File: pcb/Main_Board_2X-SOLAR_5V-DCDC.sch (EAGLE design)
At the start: 69 parts, among them CN5 USBA_FEMALE, IC1 MCP73871, IC2 MCP73871, T2 MMUN2133LT1G, U3 TPS61090RSAR, X1 Solar input, X2 5V output

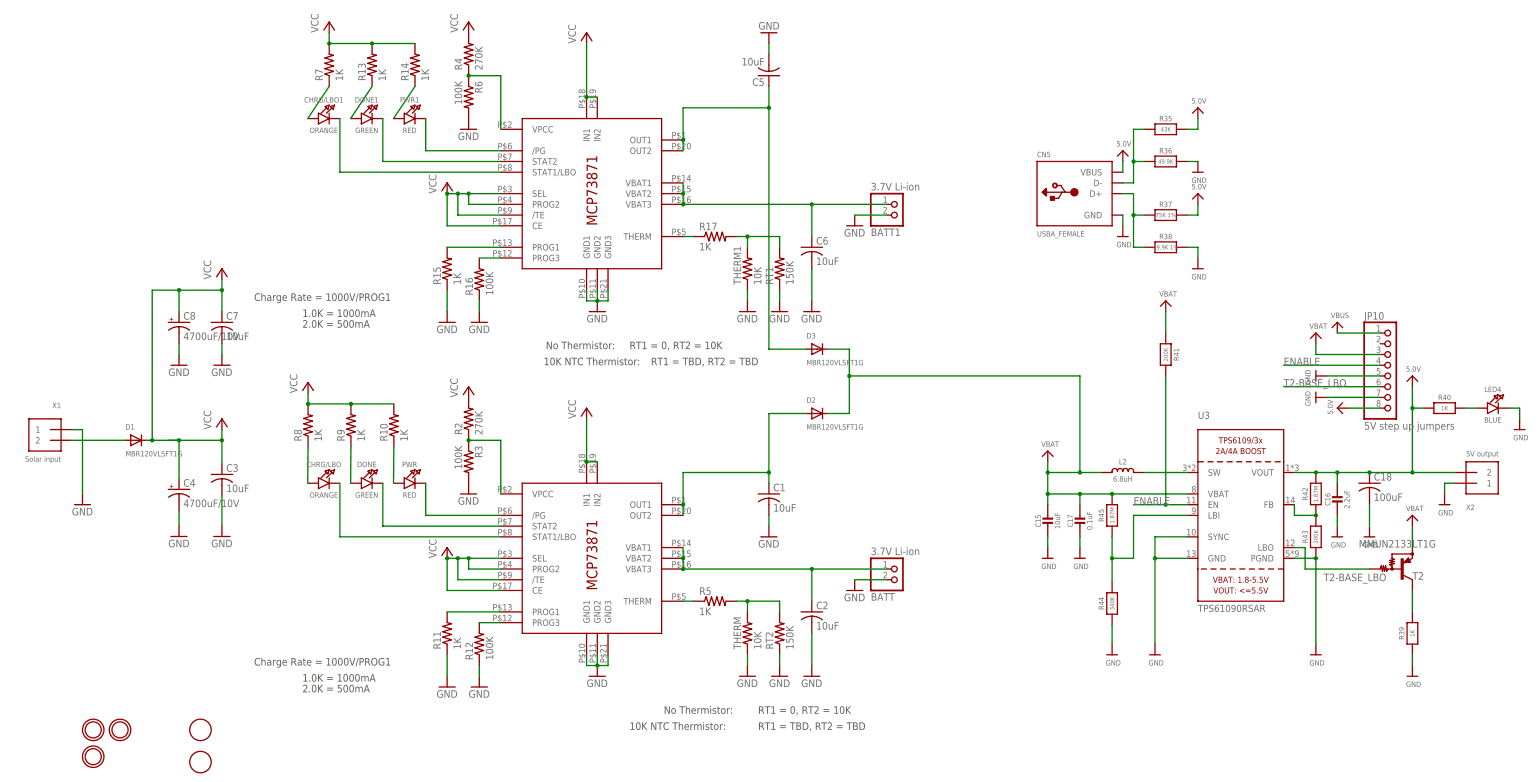
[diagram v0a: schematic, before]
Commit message: Added LT4015 footprints to eagle and began routing
LTC4015 chip footprints and schematic uploaded to eagle library. Routing started for new board. Removed all routings so only airwires exist at this point.
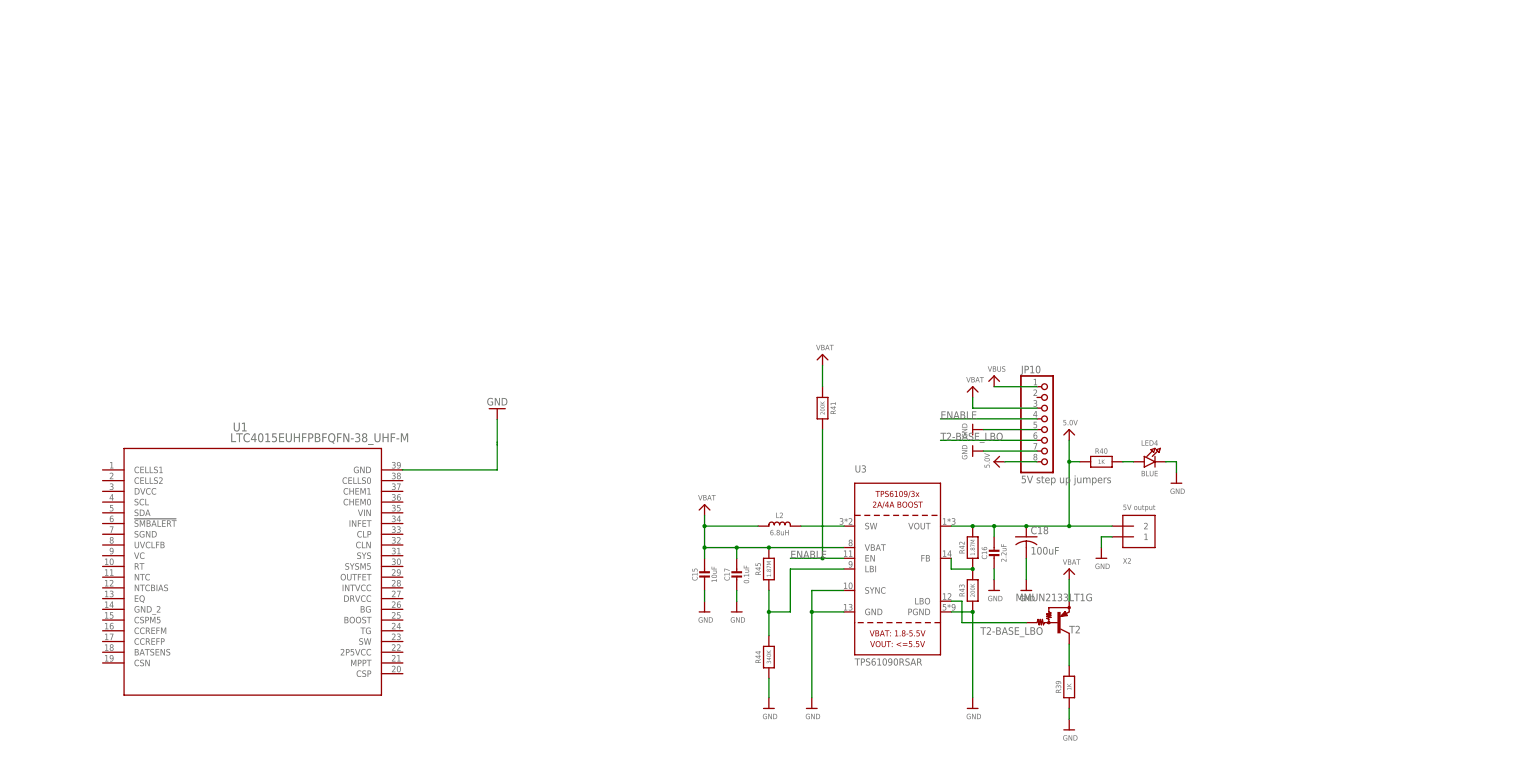
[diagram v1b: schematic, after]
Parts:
- removed BATT, BATT1: 3.7V Li-ion, adafruit:JST_2PIN-SMT-RA
- removed C1, C2, C3, C5, C6, C7: 10uF, adafruit:C-USC0805K
- removed C4, C8: 4700uF/10V, adafruit:CPOL-USE5-13
- removed CHRG/LBO, CHRG/LBO1: ORANGE, microbuilder:LED0805_NOOUTLINE
- removed CN5: USBA_FEMALE, microbuilder:USB_TYPEAPTHFML
- removed D1, D2, D3: MBR120VLSFT1G, microbuilder:DIODESOD-123
- removed DONE, DONE1: GREEN, microbuilder:LED0805_NOOUTLINE
- removed IC1, IC2: MCP73871, adafruit:MCP73871
- removed PWR, PWR1: RED, microbuilder:LED0805_NOOUTLINE
- removed R10, R13, R14, R7, R8, R9: 1K, adafruit:R-US_R0805
- removed R11, R15: 1K, adafruit:R-US_FLIPFLOP
- removed R12, R16, R3, R6: 100K, adafruit:R-US_R0805
- removed R17, R5: 1K, adafruit:R-US_M0805
- removed R2, R4: 270K, adafruit:R-US_R0805
- removed R35: 43K, microbuilder:RESISTOR0805_NOOUTLINE
- removed R36: 49.9K, microbuilder:RESISTOR0805_NOOUTLINE
- removed R37: 75K 1%, microbuilder:RESISTOR0805_NOOUTLINE
- removed R38: 49.9K 1%, microbuilder:RESISTOR0805_NOOUTLINE
- removed RT1, RT2: 150K, adafruit:R-US_M0805
- removed THERM, THERM1: 10K, adafruit:R-US_FLIPFLOP
- removed U$1, U$4, U$6: MOUNTINGHOLE2.5, microbuilder:MOUNTINGHOLE2.5
- removed U$3, U$8: FIDUCIAL, adafruit:FIDUCIAL
- removed X1: Solar input, microbuilder:TERMBLOCK_1X2
- added U1: LTC4015EUHFPBFQFN-38_UHF-M, LTC4015_LTC4015EUHF&hash_PBF:LTC4015EUHFPBFQFN-38_UHF-M
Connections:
- removed net BATT: BATT.2, C2.1, IC1.VBAT1, IC1.VBAT2, IC1.VBAT3
- removed net BATT1: BATT1.2, C6.1, IC2.VBAT1, IC2.VBAT2, IC2.VBAT3
- removed net D+1: CN5.D+, R37.1, R38.1
- removed net D-1: CN5.D-, R35.1, R36.1
- removed net N$12: CHRG/LBO.A, R8.1
- removed net N$13: DONE.A, R9.1
- removed net N$14: PWR.A, R10.1
- removed net N$19: CHRG/LBO1.A, R7.1
- removed net N$20: DONE1.A, R13.1
- removed net N$21: PWR1.A, R14.1
- removed net N$24: IC2.THERM, R17.1
- removed net N$25: R17.2, RT1.2, THERM1.2
- removed net N$5: IC1.THERM, R5.1
- removed net N$8: R5.2, RT2.2, THERM.2
- removed net PG: IC1./PG, PWR.C
- removed net PG_1: IC2./PG, PWR1.C
- removed net PROG1: IC1.PROG1, R11.2
- removed net PROG1_1: IC2.PROG1, R15.2
- removed net PROG3: IC1.PROG3, R12.2
- removed net PROG3_1: IC2.PROG3, R16.2
- removed net PV_IN: D1.A, X1.2
- removed net STAT1: CHRG/LBO.C, IC1.STAT1/LBO
- removed net STAT1_1: CHRG/LBO1.C, IC2.STAT1/LBO
- removed net STAT2: DONE.C, IC1.STAT2
- removed net STAT2_1: DONE1.C, IC2.STAT2
- removed net VCC: C3.1, C4.+, C7.1, C8.+, D1.C, IC1./TE, IC1.CE, IC1.IN1, IC1.IN2, IC1.PROG2, IC1.SEL, IC2./TE, IC2.CE, IC2.IN1, IC2.IN2, IC2.PROG2, IC2.SEL, R10.2, R13.2, R14.2, R2.2, R4.2, R7.2, R8.2, R9.2
- removed net VOUT: C1.1, D2.A, IC1.OUT1, IC1.OUT2
- removed net VOUT1: C5.1, D3.A, IC2.OUT1, IC2.OUT2
- removed net VPCC: IC1.VPCC, R2.1, R3.1
- removed net VPCC1: IC2.VPCC, R4.1, R6.1
- net 5.0V: no longer CN5.VBUS, R35.2, R37.2
- net GND: no longer BATT.1, BATT1.1, C1.2, C2.2, C3.2, C4.-, C5.2, C6.2, C7.2, C8.-, CN5.GND, IC1.GND1, IC1.GND2, IC1.GND3, IC2.GND1, IC2.GND2, IC2.GND3, R11.1, R12.1, R15.1, R16.1, R3.2, R36.2, R38.2, R6.2, RT1.1, RT2.1, THERM.1, THERM1.1, X1.1
- net VBAT: no longer D2.C, D3.C
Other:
- note removed: "1.0K = 1000mA"
- note removed: "10K NTC Thermistor:"
- note removed: "2.0K = 500mA"
- note removed: "Charge Rate = 1000V/PROG1"
- note removed: "No Thermistor:"
- note removed: "RT1 = 0, RT2 = 10K"
- note removed: "RT1 = TBD, RT2 = TBD"
- moved on the sheet: C15, C16, C17, C18, JP10, L2, LED4, R39, R40, R41, R42, R43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

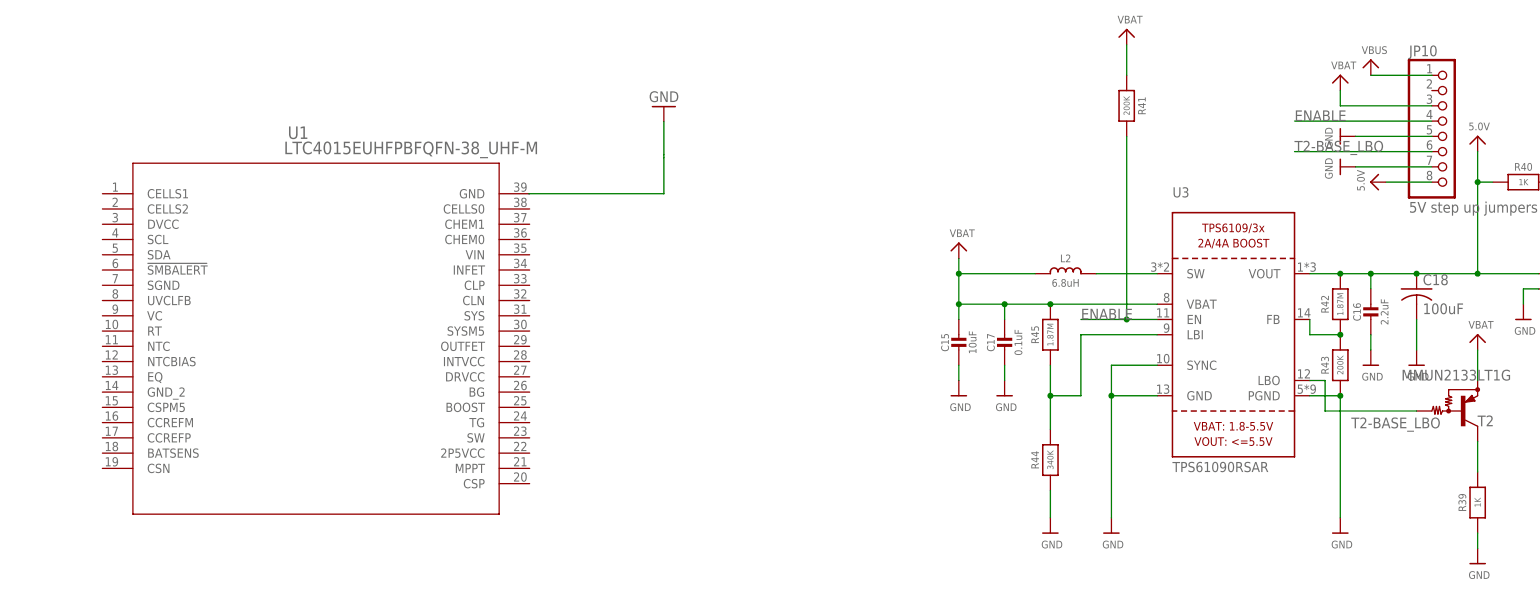
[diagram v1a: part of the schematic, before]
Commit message: Footprint added and began LTC4015 layout
Created LTC4015 footprint in library and schematic. Updated BOM for original board with prices for each part and consolidated parts
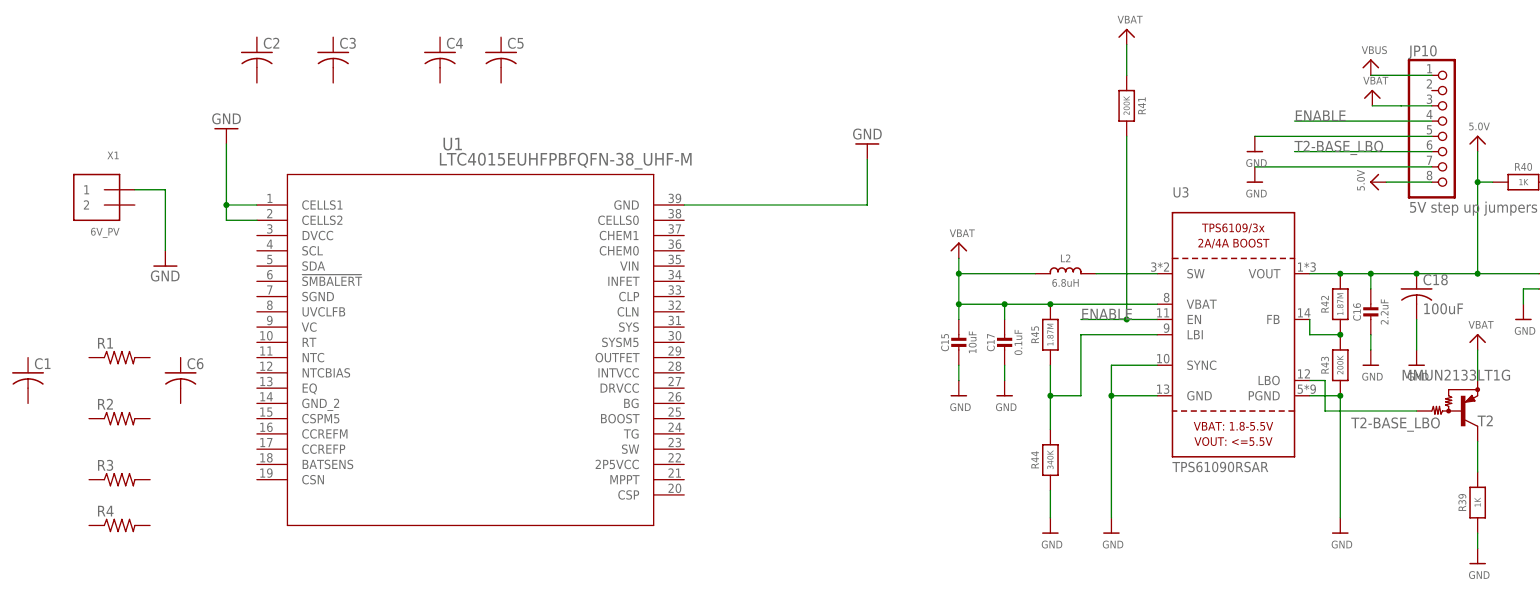
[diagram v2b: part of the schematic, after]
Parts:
- added C1, C2, C3, C4, C5, C6: (no value), adafruit:C-USC0805
- added R1, R2, R3, R4: (no value), adafruit:R-US_R0805
- added X1: 6V_PV, microbuilder:TERMBLOCK_1X2
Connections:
- net GND: now also U1.CELLS1, U1.CELLS2, U1.GND, X1.1
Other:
- moved on the sheet: U1
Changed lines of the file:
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@@
 <setting verticaltext="up"/>
 </settings>
-<grid distance="0.5" unitdist="mm" unit="mm" style="lines" multiple="1" display="no" altdistance="0.125" altunitdist="mm" altunit="mm"/>
+<grid distance="0.1" unitdist="inch" unit="inch" style="lines" multiple="1" display="no" altdistance="0.01" altunitdist="inch" altunit="inch"/>
 <layers>
 <layer number="1" name="Top" color="4" fill="1" visible="no" active="no"/>
@@
 <layer number="56" name="wert" color="7" fill="1" visible="no" active="no"/>
 <layer number="57" name="tCAD" color="7" fill="1" visible="no" active="no"/>
+<layer number="59" name="tCarbon" color="7" fill="1" visible="no" active="no"/>
+<layer number="60" name="bCarbon" color="7" fill="1" visible="no" active="no"/>
 <layer number="90" name="Modules" color="5" fill="1" visible="yes" active="yes"/>
 <layer number="91" name="Nets" color="2" fill="1" visible="yes" active="yes"/>
@@
 <layer number="127" name="_tValues" color="7" fill="1" visible="yes" active="yes"/>
 <layer number="128" name="_bValues" color="7" fill="1" visible="yes" active="yes"/>
+<layer number="129" name="Mask" color="7" fill="1" visible="yes" active="yes"/>
 <layer number="131" name="tAdjust" color="7" fill="1" visible="yes" active="yes"/>
 <layer number="132" name="bAdjust" color="7" fill="1" visible="yes" active="yes"/>
@@
 <layer number="223" name="223bmp" color="24" fill="1" visible="no" active="no"/>
 <layer number="224" name="224bmp" color="25" fill="1" visible="no" active="no"/>
+<layer number="225" name="225bmp" color="7" fill="1" visible="yes" active="yes"/>
+<layer number="226" name="226bmp" color="7" fill="1" visible="yes" active="yes"/>
+<layer number="227" name="227bmp" color="7" fill="1" visible="yes" active="yes"/>
+<layer number="228" name="228bmp" color="7" fill="1" visible="yes" active="yes"/>
+<layer number="229" name="229bmp" color="7" fill="1" visible="yes" active="yes"/>
+<layer number="230" name="230bmp" color="7" fill="1" visible="yes" active="yes"/>
 <layer number="231" name="Eagle3D_PG1" color="7" fill="1" visible="no" active="no"/>
 <layer number="232" name="Eagle3D_PG2" color="7" fill="1" visible="no" active="no"/>
@@
 <layer number="251" name="SMDround" color="7" fill="1" visible="no" active="no"/>
 <layer number="254" name="cooling" color="7" fill="1" visible="yes" active="yes"/>
+<layer number="255" name="routoute" color="7" fill="1" visible="yes" active="yes"/>
 </layers>
 <schematic xreflabel="%F%N/%S.%C%R" xrefpart="/%S.%C%R">
@@
 <part name="U1" library="LTC4015_LTC4015EUHF&amp;hash_PBF" deviceset="LTC4015EUHFPBF" device="QFN-38_UHF-M"/>
 <part name="GND" library="supply1" library_urn="urn:adsk.eagle:library:371" deviceset="GND" device=""/>
+<part name="X1" library="microbuilder" deviceset="TERMBLOCK_1X2" device="" value="6V_PV"/>
+<part name="GND1" library="supply1" library_urn="urn:adsk.eagle:library:371" deviceset="GND" device=""/>
+<part name="R1" library="adafruit" library_urn="urn:adsk.eagle:library:420" deviceset="R-US_" device="R0805"/>
+<part name="R2" library="adafruit" library_urn="urn:adsk.eagle:library:420" deviceset="R-US_" device="R0805"/>
+<part name="R3" library="adafruit" library_urn="urn:adsk.eagle:library:420" deviceset="R-US_" device="R0805"/>
+<part name="R4" library="adafruit" library_urn="urn:adsk.eagle:library:420" deviceset="R-US_" device="R0805"/>
+<part name="C1" library="adafruit" library_urn="urn:adsk.eagle:library:420" deviceset="C-US" device="C0805"/>
+<part name="C2" library="adafruit" library_urn="urn:adsk.eagle:library:420" deviceset="C-US" device="C0805"/>
+<part name="C3" library="adafruit" library_urn="urn:adsk.eagle:library:420" deviceset="C-US" device="C0805"/>
+<part name="C4" library="adafruit" library_urn="urn:adsk.eagle:library:420" deviceset="C-US" device="C0805"/>
+<part name="C5" library="adafruit" library_urn="urn:adsk.eagle:library:420" deviceset="C-US" device="C0805"/>
+<part name="C6" library="adafruit" library_urn="urn:adsk.eagle:library:420" deviceset="C-US" device="C0805"/>
+<part name="GND2" library="supply1" library_urn="urn:adsk.eagle:library:371" deviceset="GND" device=""/>
 </parts>
 <sheets>
@@
 <attribute name="VALUE" x="238.76" y="41.91" size="1.778" layer="96"/>
 </instance>
-<instance part="U$72" gate="G$1" x="228.6" y="92.71"/>
-<instance part="U$73" gate="G$1" x="228.6" y="77.47" rot="R270"/>
+<instance part="U$72" gate="G$1" x="233.934" y="90.17"/>
+<instance part="U$73" gate="G$1" x="214.376" y="74.93"/>
 <instance part="U$74" gate="G$1" x="233.68" y="74.93" rot="R90"/>
 <instance part="C18" gate="G$1" x="241.3" y="57.15"/>
-<instance part="U$81" gate="G$1" x="228.6" y="82.55" rot="R270"/>
+<instance part="U$81" gate="G$1" x="214.376" y="80.01"/>
 <instance part="JP10" gate="A" x="246.38" y="82.55"/>
 <instance part="U$82" gate="G$1" x="233.68" y="95.25"/>
-<instance part="U1" gate="A" x="20" y="73"/>
-<instance part="GND" gate="1" x="116" y="87.5" rot="R180"/>
+<instance part="U1" gate="A" x="45.72" y="71.12"/>
+<instance part="GND" gate="1" x="149.86" y="81.28" rot="R180"/>
+<instance part="X1" gate="G$1" x="22.86" y="71.12" smashed="yes" rot="MR0">
+<attribute name="VALUE" x="25.4" y="66.04" size="1.27" layer="96" rot="MR0"/>
+<attribute name="NAME" x="25.4" y="78.74" size="1.27" layer="95" rot="MR0"/>
+</instance>
+<instance part="GND1" gate="1" x="33.02" y="60.96"/>
+<instance part="R1" gate="G$1" x="25.4" y="45.72"/>
+<instance part="R2" gate="G$1" x="25.4" y="35.56"/>
+<instance part="R3" gate="G$1" x="25.4" y="25.4"/>
+<instance part="R4" gate="G$1" x="25.4" y="17.78"/>
+<instance part="C1" gate="G$1" x="10.16" y="43.18"/>
+<instance part="C2" gate="G$1" x="48.26" y="96.52"/>
+<instance part="C3" gate="G$1" x="60.96" y="96.52"/>
+<instance part="C4" gate="G$1" x="78.74" y="96.52"/>
+<instance part="C5" gate="G$1" x="88.9" y="96.52"/>
+<instance part="C6" gate="G$1" x="35.56" y="43.18"/>
+<instance part="GND2" gate="1" x="43.18" y="83.82" rot="R180"/>
 </instances>
 <busses>
@@
 <segment>
 <pinref part="U$73" gate="G$1" pin="GND"/>
-<wire x1="243.84" y1="77.47" x2="231.14" y2="77.47" width="0.1524" layer="91"/>
+<wire x1="243.84" y1="77.47" x2="214.376" y2="77.47" width="0.1524" layer="91"/>
 <pinref part="JP10" gate="A" pin="7"/>
 </segment>
@@
 <pinref part="U$81" gate="G$1" pin="GND"/>
 <pinref part="JP10" gate="A" pin="5"/>
-<wire x1="231.14" y1="82.55" x2="243.84" y2="82.55" width="0.1524" layer="91"/>
+<wire x1="214.376" y1="82.55" x2="243.84" y2="82.55" width="0.1524" layer="91"/>
 </segment>
 <segment>
@@
 </segment>
 <segment>
-<wire x1="93.5" y1="73" x2="116" y2="73" width="0.1524" layer="91"/>
-<wire x1="116" y1="73" x2="116" y2="79" width="0.1524" layer="91"/>
+<pinref part="U1" gate="A" pin="GND"/>
+<wire x1="119.38" y1="71.12" x2="149.86" y2="71.12" width="0.1524" layer="91"/>
 <pinref part="GND" gate="1" pin="GND"/>
-<wire x1="116" y1="79" x2="116" y2="79.5" width="0.1524" layer="91"/>
-<wire x1="116" y1="79.5" x2="116" y2="84.96" width="0.1524" layer="91"/>
+<wire x1="149.86" y1="71.12" x2="149.86" y2="78.74" width="0.1524" layer="91"/>
+</segment>
+<segment>
+<pinref part="X1" gate="G$1" pin="1"/>
+<wire x1="27.94" y1="73.66" x2="33.02" y2="73.66" width="0.1524" layer="91"/>
+<pinref part="GND1" gate="1" pin="GND"/>
+<wire x1="33.02" y1="73.66" x2="33.02" y2="63.5" width="0.1524" layer="91"/>
+</segment>
+<segment>
+<pinref part="U1" gate="A" pin="CELLS2"/>
+<wire x1="48.26" y1="68.58" x2="43.18" y2="68.58" width="0.1524" layer="91"/>
+<wire x1="43.18" y1="68.58" x2="43.18" y2="71.12" width="0.1524" layer="91"/>
+<pinref part="U1" gate="A" pin="CELLS1"/>
+<wire x1="43.18" y1="71.12" x2="43.18" y2="81.28" width="0.1524" layer="91"/>
+<wire x1="48.26" y1="71.12" x2="43.18" y2="71.12" width="0.1524" layer="91"/>
+<junction x="43.18" y="71.12"/>
+<pinref part="GND2" gate="1" pin="GND"/>
 </segment>
 </net>
@@
 <pinref part="U$72" gate="G$1" pin="VBAT"/>
 <pinref part="JP10" gate="A" pin="3"/>
-<wire x1="228.6" y1="90.17" x2="228.6" y2="87.63" width="0.1524" layer="91"/>
-<wire x1="228.6" y1="87.63" x2="243.84" y2="87.63" width="0.1524" layer="91"/>
-</segment>
-<segment>
+<wire x1="233.934" y1="87.63" x2="238.76" y2="87.63" width="0.1524" layer="91"/>
+<wire x1="238.76" y1="87.63" x2="243.84" y2="87.63" width="0.1524" layer="91"/>
+</segment>
+<segment>
